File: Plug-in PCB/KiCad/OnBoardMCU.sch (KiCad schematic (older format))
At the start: 25 parts, among them J14 Conn_01x01, J16 Conn_01x01, J18 Conn_01x08, U4 ATSAME70N21A-CN, Y1 ABM8G-12.000MHZ-4Y-T3

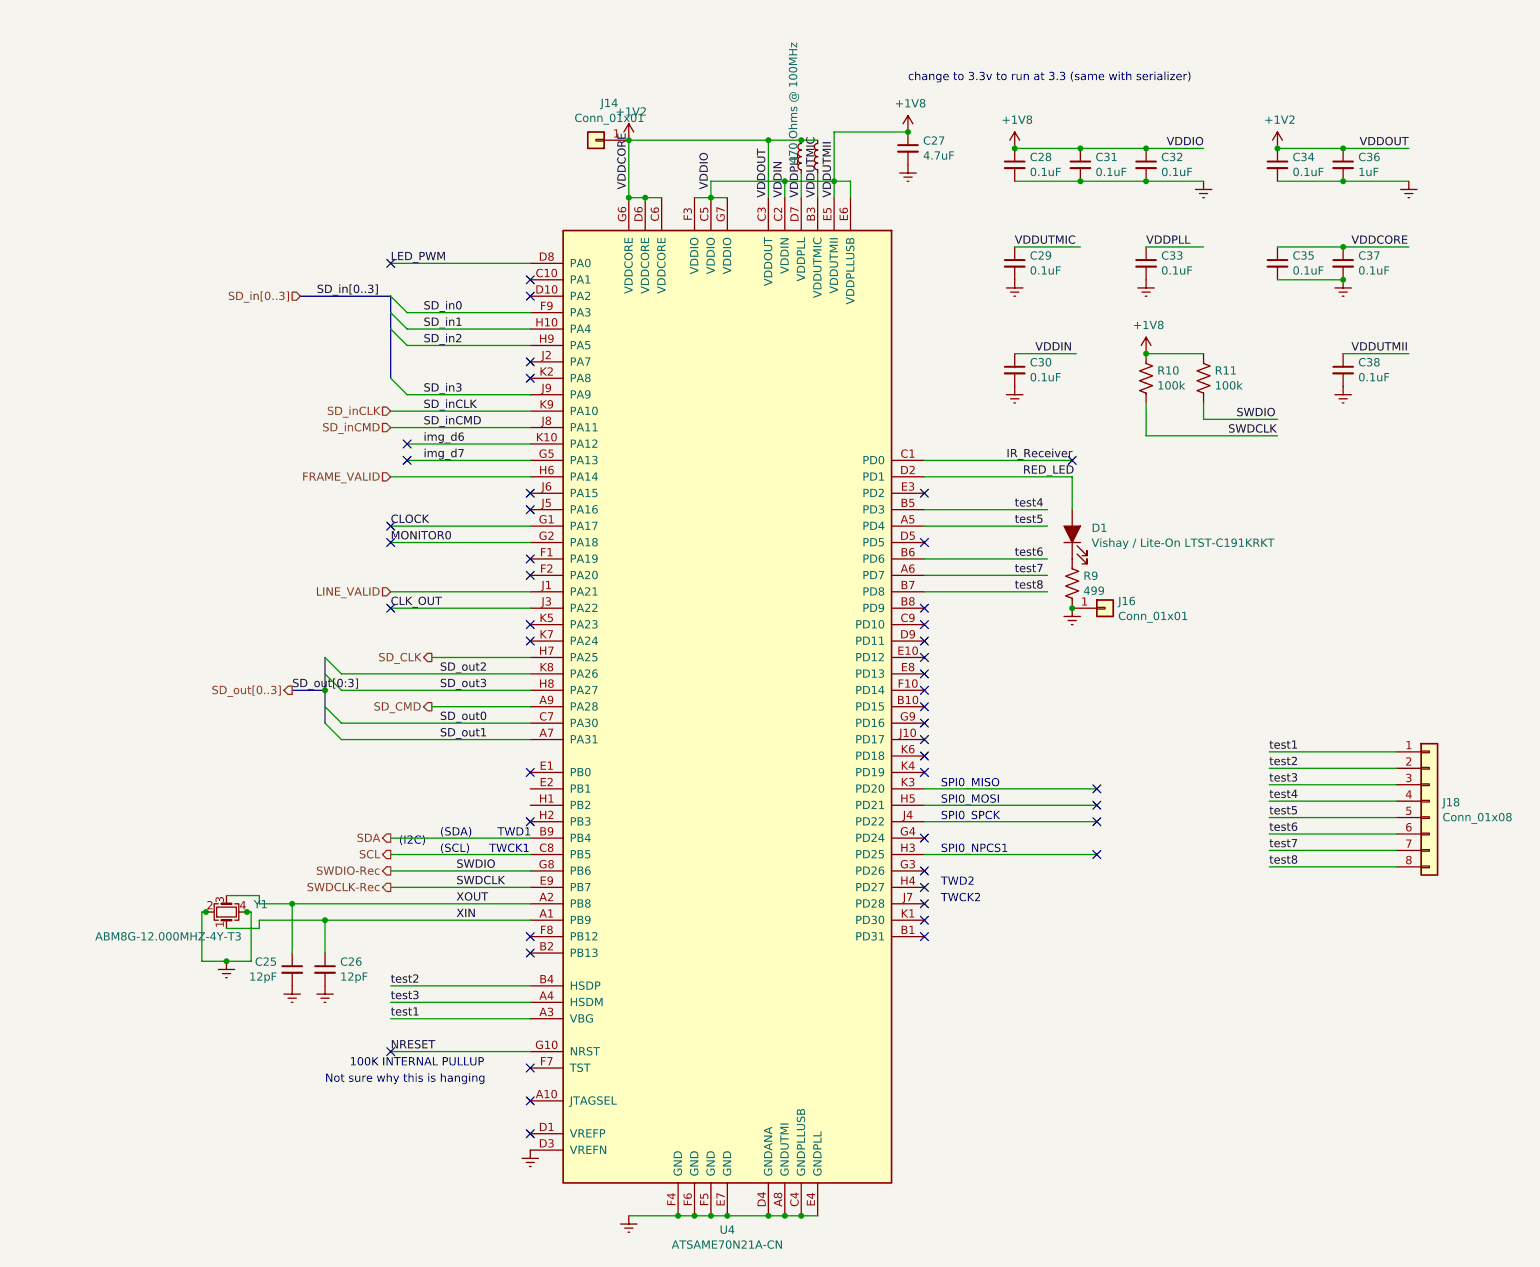
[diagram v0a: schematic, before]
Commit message: Wired Expansion Board Update
1. Begin hardcoding bit-bang communication between wirefree MCU and wired expansion MCU.
++ Can I use the PIO module on the pins to send data in sync while grabbing image from the sensor with parallel capture mode?

2. Wired expansion board schematics and layout modifications
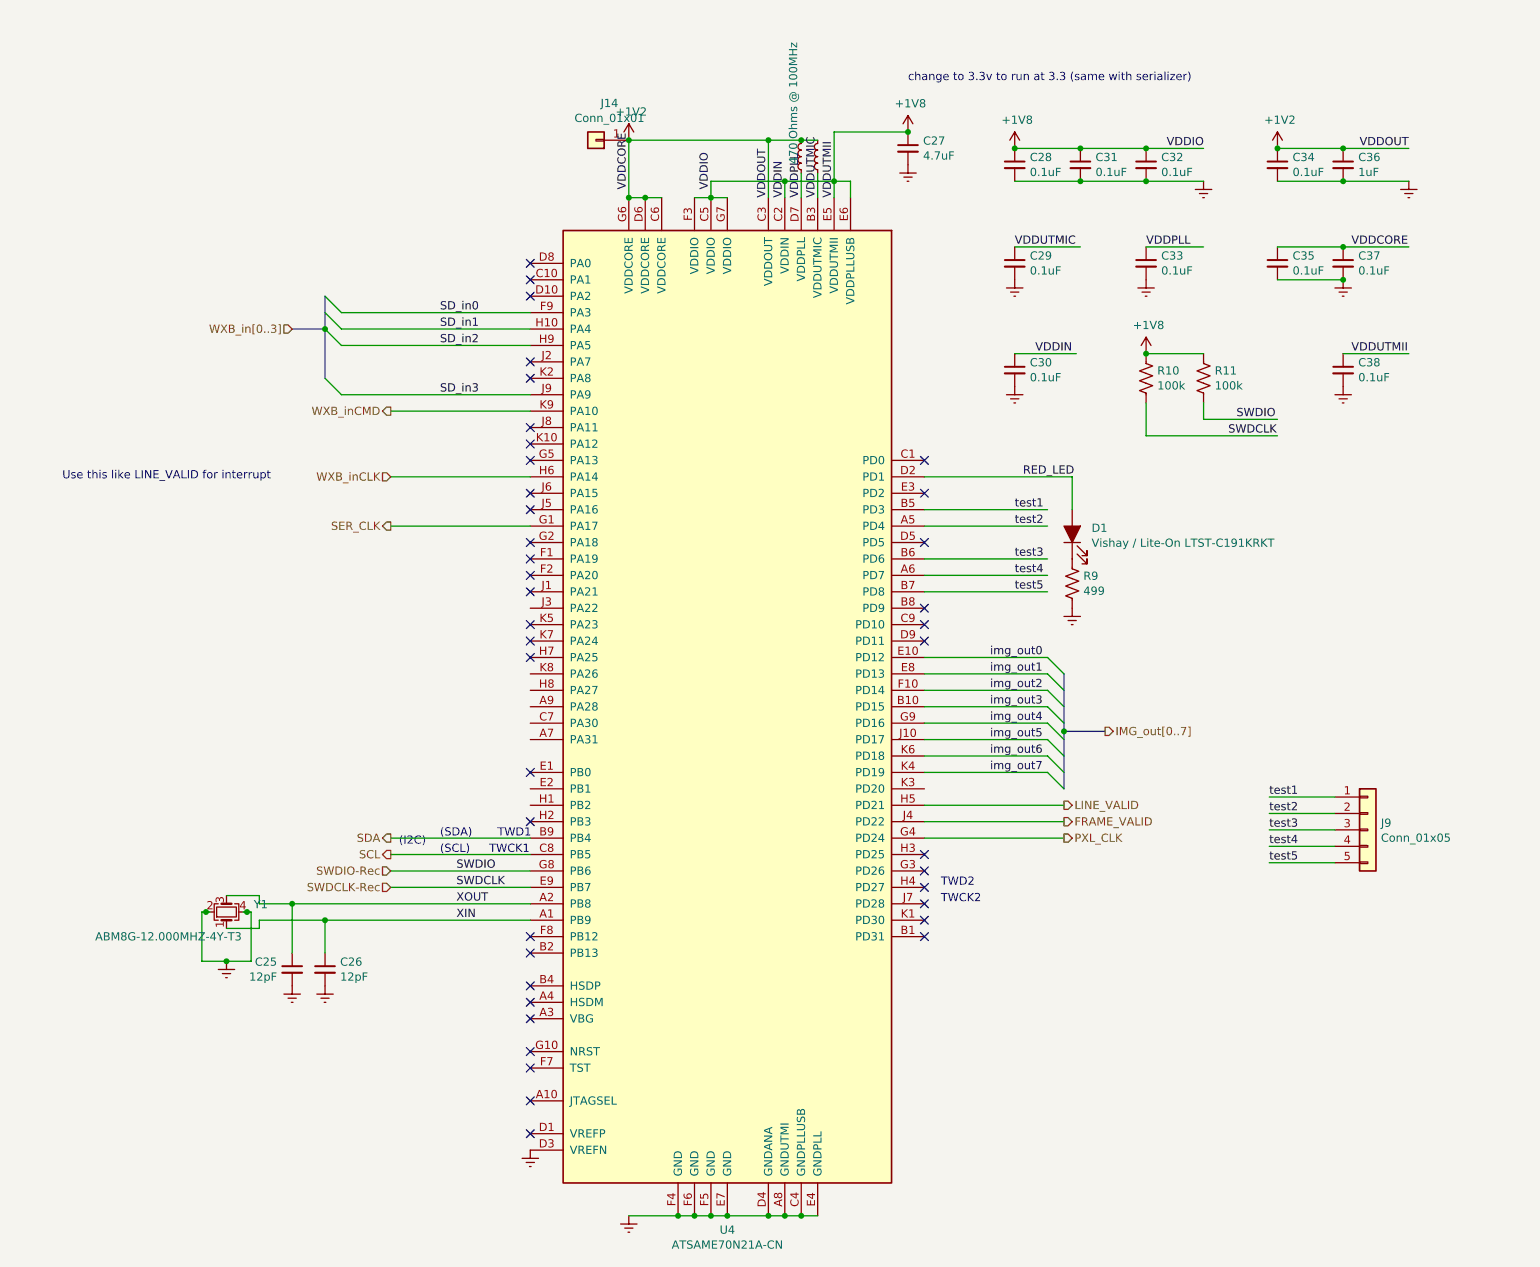
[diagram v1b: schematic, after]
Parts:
- removed J16: Conn_01x01, .Connector:Conn_1x1_700_Circular_Pad, symbol .Connector:Conn_01x01
- removed J18: Conn_01x08, Connector_PinHeader_2.54mm:PinHeader_1x08_P2.54mm_Vertical, symbol Connector_Generic:Conn_01x08
- added J9: Conn_01x05, Connector_PinHeader_1.27mm:PinHeader_1x05_P1.27mm_Vertical, symbol Connector_Generic:Conn_01x05
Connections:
- net labels added: IMG_out[0..7], PXL_CLK, SER_CLK, WXB_inCLK, WXB_inCMD, WXB_in[0..3], img_out0, img_out1, img_out2, img_out3, img_out4, img_out5, img_out6, img_out7
- net labels removed: CLK_OUT, CLOCK, IR_Receiver, LED_PWM, MONITOR0, NRESET, SD_CLK, SD_CMD, SD_inCLK, SD_inCMD, SD_in[0..3], SD_out0, SD_out1, SD_out2, SD_out3, SD_out[0..3], SD_out[0:3], img_d6, img_d7, test6, test7, test8
- wire segments 116 -> 102
- no-connect marks 48 -> 40
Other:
- note added: "Use this like LINE_VALID for interrupt"
- note removed: "100K INTERNAL PULLUP"
- note removed: "Not sure why this is hanging"
- note removed: "SPI0_MISO"
- note removed: "SPI0_MOSI"
- note removed: "SPI0_NPCS1"
- note removed: "SPI0_SPCK"

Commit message: Wired Expansion Board Updates
1. KiCad: Schematics and layouts completed/Gerber files generated
2. Atmel: Communication protocol from WireFree to WiredExpansion written
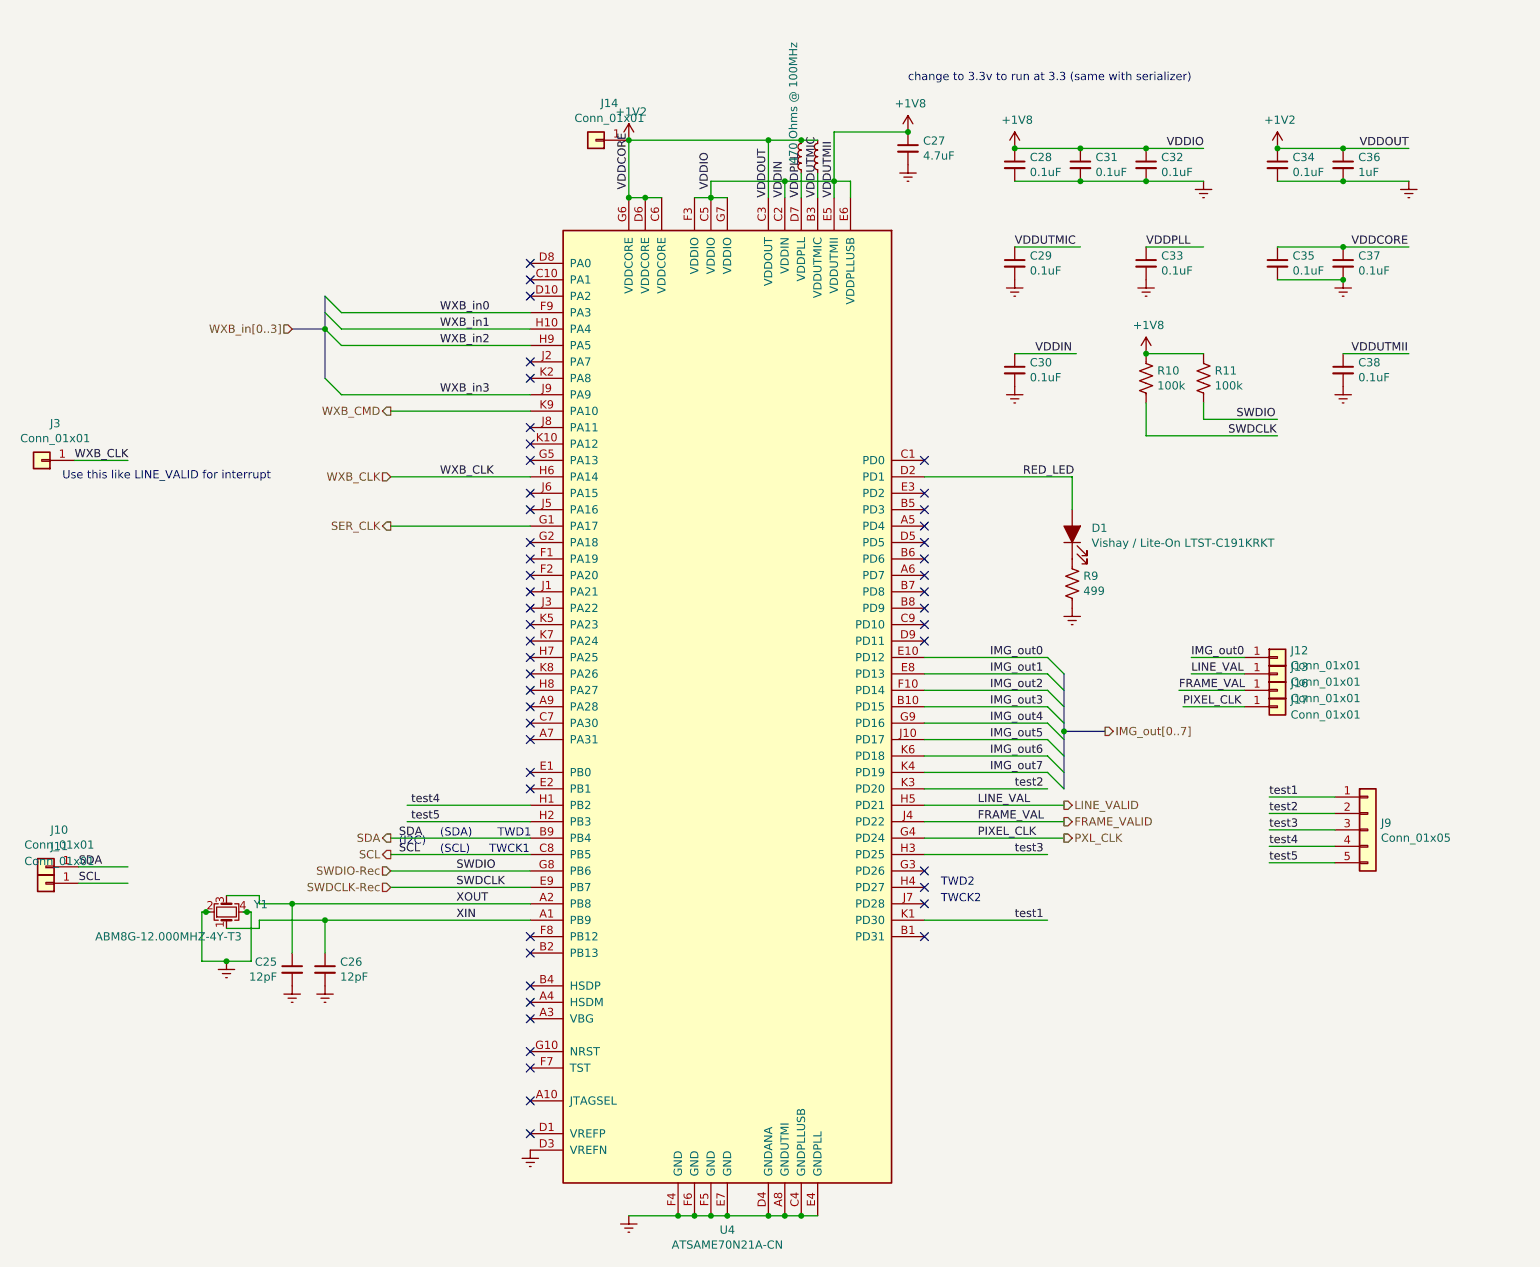
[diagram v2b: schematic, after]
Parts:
- added J10, J11, J12, J13, J16, J17, J3: Conn_01x01, Connector_PinHeader_1.27mm:PinHeader_1x01_P1.27mm_Vertical, symbol .Connector:Conn_01x01
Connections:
- net labels added: FRAME_VAL, IMG_out0, IMG_out1, IMG_out2, IMG_out3, IMG_out4, IMG_out5, IMG_out6, IMG_out7, LINE_VAL, PIXEL_CLK, WXB_CLK, WXB_CMD, WXB_in0, WXB_in1, WXB_in2, WXB_in3
- net labels removed: SD_in0, SD_in1, SD_in2, SD_in3, WXB_inCLK, WXB_inCMD, img_out0, img_out1, img_out2, img_out3, img_out4, img_out5, img_out6, img_out7
- wire segments 102 -> 109
- no-connect marks 40 -> 49
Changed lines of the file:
@@
 $Descr A4 11693 8268
 encoding utf-8
-Sheet 5 6
+Sheet 6 6
 Title ""
 Date ""
@@
 	3100 2150 3200 2250
 Text Label 3800 1950 0    50   ~ 0
-SD_in2
+WXB_in2
 Text Label 3800 2250 0    50   ~ 0
-SD_in3
+WXB_in3
 Text Label 3800 1750 0    50   ~ 0
-SD_in0
+WXB_in0
 Text Label 3800 1850 0    50   ~ 0
-SD_in1
+WXB_in1
 NoConn ~ 4350 4550
 $Comp
@@
 NoConn ~ 4350 6350
 NoConn ~ 4350 5650
-NoConn ~ 4350 4850
 Wire Wire Line
 	4350 5150 3500 5150
@@
 NoConn ~ 6750 5250
 NoConn ~ 6750 5350
-NoConn ~ 6750 5450
 NoConn ~ 6750 5550
 Wire Wire Line
@@
 	7650 2950 7650 2750
 Text HLabel 3500 2750 0    50   Input ~ 0
-WXB_inCLK
+WXB_CLK
 Text HLabel 3500 5150 0    50   Input ~ 0
 SWDIO-Rec
@@
 $EndComp
 Wire Wire Line
-	6750 2950 7500 2950
-Wire Wire Line
-	6750 3050 7500 3050
-Wire Wire Line
-	6750 3250 7500 3250
-Wire Wire Line
-	6750 3350 7500 3350
-Wire Wire Line
-	6750 3450 7500 3450
-Text Label 7300 2950 0    50   ~ 0
+	6750 5450 7500 5450
+Wire Wire Line
+	6750 4650 7500 4650
+Wire Wire Line
+	6750 5050 7500 5050
+Wire Wire Line
+	4350 4750 3600 4750
+Wire Wire Line
+	4350 4850 3600 4850
+Text Label 7300 5450 0    50   ~ 0
 test1
 Text Label 8850 5000 0    50   ~ 0
@@
 Text HLabel 7600 4950 2    50   Output ~ 0
 PXL_CLK
-Text Label 7150 3850 0    50   ~ 0
-img_out0
-Text Label 7150 3950 0    50   ~ 0
-img_out1
-Text Label 7150 4050 0    50   ~ 0
-img_out2
-Text Label 7150 4150 0    50   ~ 0
-img_out3
-Text Label 7150 4250 0    50   ~ 0
-img_out4
-Text Label 7150 4350 0    50   ~ 0
-img_out5
-Text Label 7150 4450 0    50   ~ 0
-img_out6
-Text Label 7150 4550 0    50   ~ 0
-img_out7
 NoConn ~ 4350 1450
 Wire Wire Line
@@
 Text HLabel 3500 3050 0    50   Output ~ 0
 SER_CLK
-NoConn ~ 6750 5050
 NoConn ~ 4350 6250
 NoConn ~ 6750 2650
@@
 NoConn ~ 4350 5950
 NoConn ~ 4350 6050
-Text Label 7300 3050 0    50   ~ 0
+Text Label 7300 4650 0    50   ~ 0
 test2
-Text Label 7300 3250 0    50   ~ 0
+Text Label 7300 5050 0    50   ~ 0
 test3
-Text Label 7300 3350 0    50   ~ 0
+Text Label 3800 4750 2    50   ~ 0
 test4
-Text Label 7300 3450 0    50   ~ 0
+Text Label 3800 4850 2    50   ~ 0
 test5
 Wire Wire Line
@@
 Wire Wire Line
 	3500 2350 4350 2350
+Text HLabel 3500 2350 0    50   Output ~ 0
+WXB_CMD
+Text Label 7150 3850 0    50   ~ 0
+IMG_out0
+Text Label 7150 3950 0    50   ~ 0
+IMG_out1
+Text Label 7150 4050 0    50   ~ 0
+IMG_out2
+Text Label 7150 4150 0    50   ~ 0
+IMG_out3
+Text Label 7150 4250 0    50   ~ 0
+IMG_out4
+Text Label 7150 4350 0    50   ~ 0
+IMG_out5
+Text Label 7150 4450 0    50   ~ 0
+IMG_out6
+Text Label 7150 4550 0    50   ~ 0
+IMG_out7
+NoConn ~ 6750 2950
+NoConn ~ 6750 3050
+NoConn ~ 4350 4650
+NoConn ~ 6750 3250
+NoConn ~ 6750 3350
+NoConn ~ 6750 3450
+NoConn ~ 4350 3950
+NoConn ~ 4350 4050
+NoConn ~ 4350 4150
+NoConn ~ 4350 4250
+NoConn ~ 4350 4350
+NoConn ~ 4350 3550
+$Comp
+L .Connector:Conn_01x01 J11
+U 1 1 5D3867A6
+P 1400 5225
+F 0 "J11" H 1318 5000 50  0000 C CNN
+F 1 "Conn_01x01" H 1318 5091 50  0000 C CNN
+F 2 "Connector_PinHeader_1.27mm:PinHeader_1x01_P1.27mm_Vertical" H 1400 5225 50  0001 C CNN
+F 3 "~" H 1400 5225 50  0001 C CNN
+	1    1400 5225
+	-1   0    0    1
+$EndComp
+$Comp
+L .Connector:Conn_01x01 J10
+U 1 1 5D387447
+P 1400 5125
+F 0 "J10" H 1318 4900 50  0000 C CNN
+F 1 "Conn_01x01" H 1318 4991 50  0000 C CNN
+F 2 "Connector_PinHeader_1.27mm:PinHeader_1x01_P1.27mm_Vertical" H 1400 5125 50  0001 C CNN
+F 3 "~" H 1400 5125 50  0001 C CNN
+	1    1400 5125
+	-1   0    0    1
+$EndComp
+Wire Wire Line
+	1600 5125 1900 5125
+Wire Wire Line
+	1600 5225 1900 5225
+Text Label 1600 5125 0    50   ~ 0
+SDA
+Text Label 1600 5225 0    50   ~ 0
+SCL
+$Comp
+L .Connector:Conn_01x01 J12
+U 1 1 5D390F27
+P 8900 3850
+F 0 "J12" H 8980 3892 50  0000 L CNN
+F 1 "Conn_01x01" H 8980 3801 50  0000 L CNN
+F 2 "Connector_PinHeader_1.27mm:PinHeader_1x01_P1.27mm_Vertical" H 8900 3850 50  0001 C CNN
+F 3 "~" H 8900 3850 50  0001 C CNN
+	1    8900 3850
+	1    0    0    -1
+$EndComp
+Text Label 8375 3850 0    50   ~ 0
+IMG_out0
+Wire Wire Line
+	8375 3850 8700 3850
+$Comp
+L .Connector:Conn_01x01 J13
+U 1 1 5D39AD49
+P 8900 3950
+F 0 "J13" H 8980 3992 50  0000 L CNN
+F 1 "Conn_01x01" H 8980 3901 50  0000 L CNN
+F 2 "Connector_PinHeader_1.27mm:PinHeader_1x01_P1.27mm_Vertical" H 8900 3950 50  0001 C CNN
+F 3 "~" H 8900 3950 50  0001 C CNN
+	1    8900 3950
+	1    0    0    -1
+$EndComp
+$Comp
+L .Connector:Conn_01x01 J16
+U 1 1 5D39AFB3
+P 8900 4050
+F 0 "J16" H 8980 4092 50  0000 L CNN
+F 1 "Conn_01x01" H 8980 4001 50  0000 L CNN
+F 2 "Connector_PinHeader_1.27mm:PinHeader_1x01_P1.27mm_Vertical" H 8900 4050 50  0001 C CNN
+F 3 "~" H 8900 4050 50  0001 C CNN
+	1    8900 4050
+	1    0    0    -1
+$EndComp
+Text Label 8375 3950 0    50   ~ 0
+LINE_VAL
+Text Label 8300 4050 0    50   ~ 0
+FRAME_VAL
+$Comp
+L .Connector:Conn_01x01 J17
+U 1 1 5D3AE3FD
+P 8900 4150
+F 0 "J17" H 8980 4192 50  0000 L CNN
+F 1 "Conn_01x01" H 8980 4101 50  0000 L CNN
+F 2 "Connector_PinHeader_1.27mm:PinHeader_1x01_P1.27mm_Vertical" H 8900 4150 50  0001 C CNN
+F 3 "~" H 8900 4150 50  0001 C CNN
+	1    8900 4150
+	1    0    0    -1
+$EndComp
+Text Label 8325 4150 0    50   ~ 0
+PIXEL_CLK
+Text Label 7075 4750 0    50   ~ 0
+LINE_VAL
+Text Label 7075 4850 0    50   ~ 0
+FRAME_VAL
+Text Label 7075 4950 0    50   ~ 0
+PIXEL_CLK
+Wire Wire Line
+	8325 4150 8700 4150
+Wire Wire Line
+	8300 4050 8700 4050
+Wire Wire Line
+	8375 3950 8700 3950
+$Comp
+L .Connector:Conn_01x01 J3
+U 1 1 5D3CB757
+P 1375 2650
+F 0 "J3" H 1293 2425 50  0000 C CNN
+F 1 "Conn_01x01" H 1293 2516 50  0000 C CNN
+F 2 "Connector_PinHeader_1.27mm:PinHeader_1x01_P1.27mm_Vertical" H 1375 2650 50  0001 C CNN
+F 3 "~" H 1375 2650 50  0001 C CNN
+	1    1375 2650
+	-1   0    0    1
+$EndComp
+Text Label 1575 2650 0    50   ~ 0
+WXB_CLK
+Wire Wire Line
+	1575 2650 1900 2650
 Wire Bus Line
 	3100 1650 3100 1850
@@
 Wire Bus Line
 	7600 3950 7600 4300
-Text HLabel 3500 2350 0    50   Output ~ 0
-WXB_inCMD
+Text Label 3800 2750 0    50   ~ 0
+WXB_CLK
+Text Label 3550 4950 0    50   ~ 0
+SDA
+Text Label 3550 5050 0    50   ~ 0
+SCL
 $EndSCHEMATC
